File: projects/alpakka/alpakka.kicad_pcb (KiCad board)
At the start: 2 copper layers, 130 x 51 mm, 94 parts, among them P1 Debug, P2 Endpoint, P3 Conn_01x02, Q1 Q_PMOS_DGS, U1 Raspberry_Pico, U10 ST_LSM6, U12 ST_LSM6, U2 Alpsalpine_RKJXV, U3 Alpsalpine_EC10E, U4 Alpsalpine_RKJXM, U6 NXP_PCAL6416A, U8 NXP_PCAL6416A

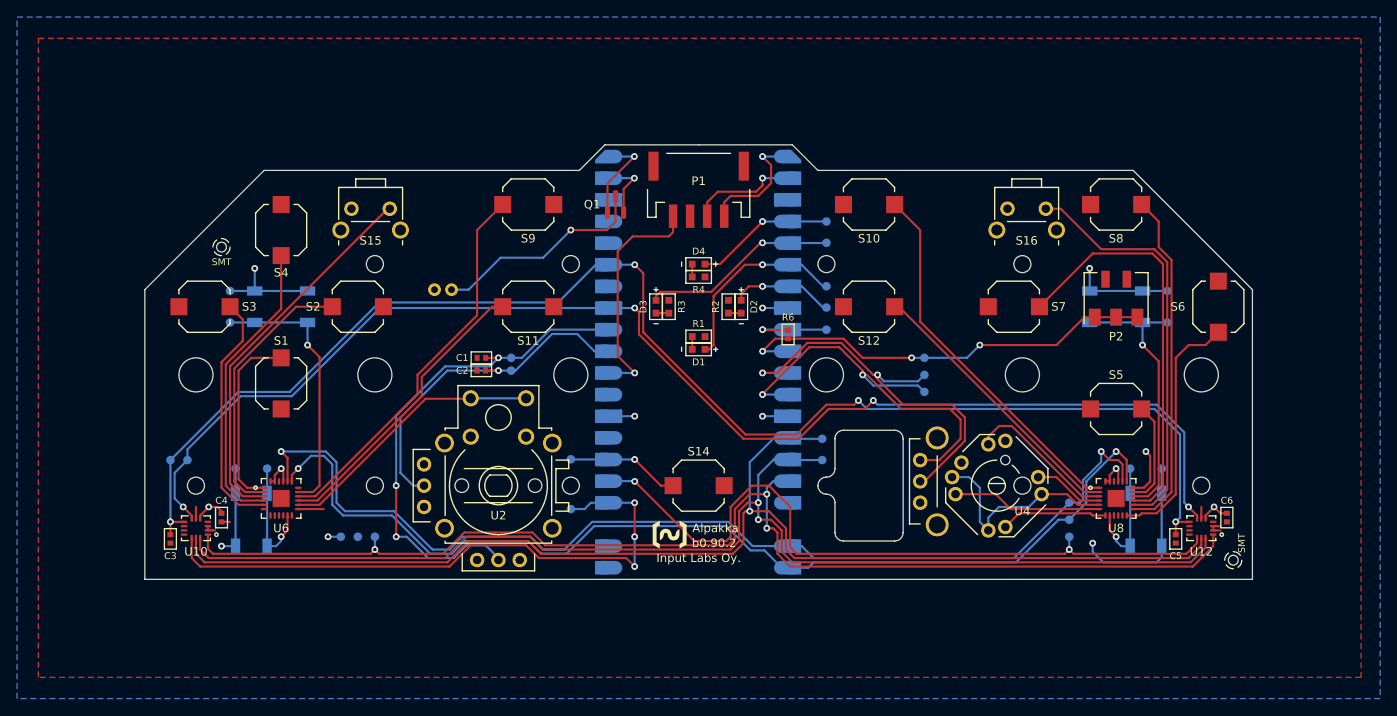
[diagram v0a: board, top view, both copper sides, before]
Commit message: Longmao's dual_thumbstick_mod_for_rp2040_picomini
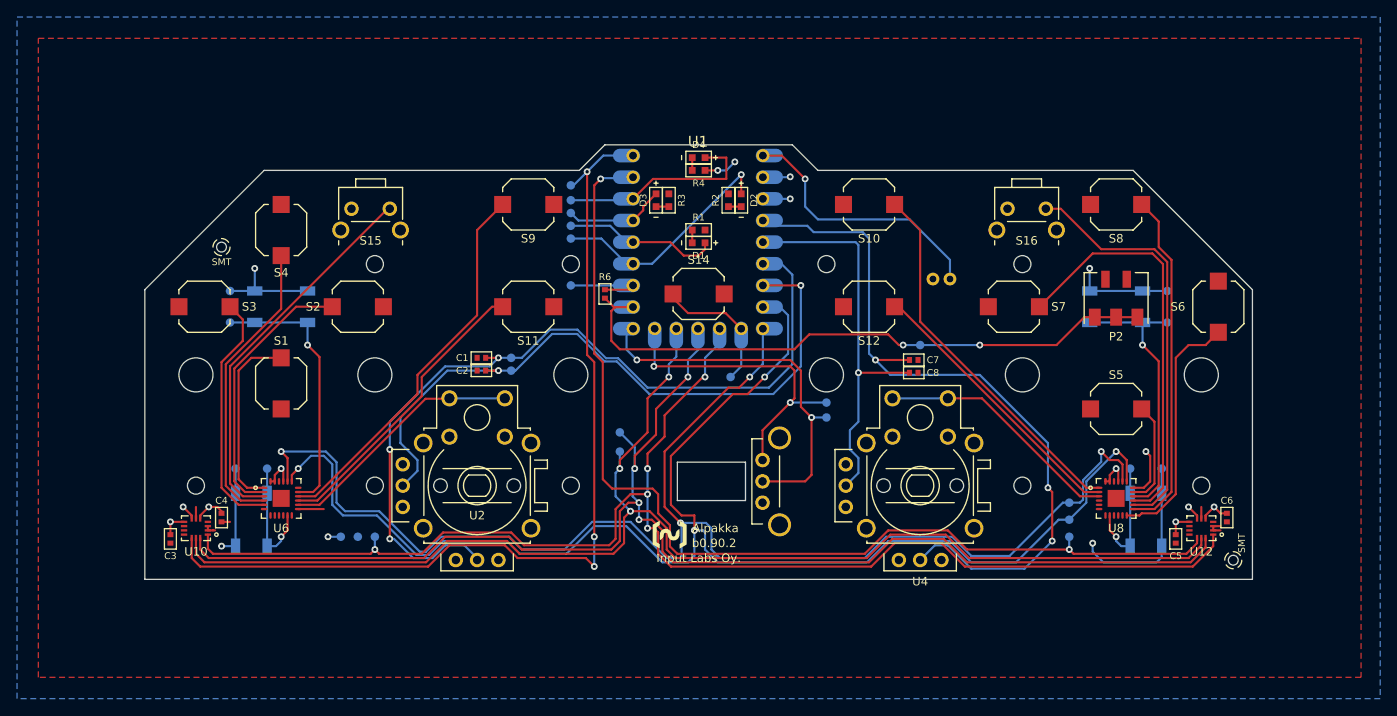
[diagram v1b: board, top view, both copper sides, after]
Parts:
- removed P1: Debug, ILO_fp:JST_S4B-PH-SM4-K-TB
- removed Q1: Q_PMOS_DGS, ILO_fp:SOT-23-DGS
- removed TP33, TP35: Endpoint, ILO_fp:Pad_1mm
- added C7: C, ILO_fp:0402, F.Cu at (125.2, 60.2)
- added C8: C, ILO_fp:0402, F.Cu at (125.2, 61.8)
- U1: value Raspberry_Pico -> 微雪RP2040-ZERO; footprint ILO_fp:Raspberry_Pico -> ILO_fp:PICOMINI
- U4: value Alpsalpine_RKJXM -> Alpsalpine_RKJXV; footprint ILO_fp:Alpsalpine_RKJXM1015004 -> ILO_fp:Alpsalpine_RKJXV122400R
- moved P3 58.5 mm to (128.5, 50.8)
- moved TP0 38.0 mm to (85.0, 39.8)
- moved TP5 31.1 mm to (85.0, 46.0)
- moved TP4 30.8 mm to (85.0, 44.5)
- moved TP6 30.4 mm to (85.0, 51.5)
- moved TP3 30.2 mm to (85.0, 43.0)
- moved TP2 30.1 mm to (85.0, 41.5)
- moved TP11 24.0 mm to (90.8, 68.8)
- moved TP10 23.8 mm to (90.8, 71.0)
- moved S14 22.5 mm to (100.0, 52.5)
- moved R6 22.0 mm to (89.0, 52.5)
- moved TP13 21.1 mm to (103.8, 62.2)
- moved U3 18.5 mm to (108.5, 74.5)
- moved U1 15.1 mm to (100.8, 45.8), turned to 180 degrees
- moved TP8 12.5 mm to (115.0, 67.0)
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- renumbered TP24 to TP0, TP25 to TP1, TP14 to TP10, TP15 to TP11, TP16 to TP12, TP26 to TP13, TP19 to TP14, TP20 to TP15, TP4 to TP2, TP31 to TP26, TP32 to TP27, TP5 to TP3, TP36 to TP3V3, TP6 to TP4, TP7 to TP5, TP9 to TP6, TP10 to TP7, TP11 to TP8, TP12 to TP9, TP3 to TPGND1
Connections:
- C3 pad 2: VCCA -> VCC
- C5 pad 2: VCCA -> VCC
- P3 pad 1: BAT -> 5V
- U1 pad 1: UART_TX -> CS1
- U1 pad 10: GP7 -> SPI_CK
- U1 pad 11: GP8 -> SPI_TX
- U1 pad 12: GP9 -> SPI_RX
- U1 pad 13: GND -> GP20
- U1 pad 14: SPI_CK -> I2C_SDA
- U1 pad 15: SPI_TX -> I2C_SCL
- U1 pad 16: SPI_RX -> ADC0
- U1 pad 17: unconnected-(U1-GP_13-Pad17) -> ADC1
- U1 pad 19: I2C_SDA -> ADC3
- U1 pad 2: UART_RX -> GP2
- U1 pad 20: I2C_SCL -> VCC
- U1 pad 21: unconnected-(U1-GP_16-Pad21) -> GND
- U1 pad 22: unconnected-(U1-GP_17-Pad22) -> 5V
- U1 pad 3: unconnected-(U1-GND-Pad3) -> GP3
- U1 pad 4: GP2 -> GP4
- U1 pad 5: GP3 -> GP5
- U1 pad 6: GP4 -> GP6
- U1 pad 7: GP5 -> GP7
- U1 pad 8: GND -> GP8
- U1 pad 9: GP6 -> GP9
- U10 pad 7: GNDA -> GND
- U10 pad 8: VCCA -> VCC
- U12 pad 7: GNDA -> GND
- U12 pad 8: VCCA -> VCC
- U4 pad 1: B6 -> GND
- U4 pad 2: B3 -> ADC2
- U4 pad 3: B2 -> VCC
- U4 pad 4: B5 -> GND
- U4 pad 5: B4 -> ADC3
- U4 pad 6: GND -> VCC
- U8 pad 4: B3 -> unconnected-(U8-P3-Pad4)
- U8 pad 5: B4 -> unconnected-(U8-P4-Pad5)
- U8 pad 6: B5 -> unconnected-(U8-P5-Pad6)
- U8 pad 7: B6 -> unconnected-(U8-P6-Pad7)
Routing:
- net VCCA: track 167.5 -> 0.00 mm, vias 4 -> 0
- net GNDA: track 155.4 -> 0.00 mm, vias 4 -> 0
- net ADC3: track 0.00 -> 85.8 mm, vias 0 -> 3
- net ADC2: track 0.00 -> 46.3 mm, vias 0 -> 1
- net I2C_SCL: track 121.9 -> 166.9 mm, vias 2 -> 4
- net ADC0: track 40.0 -> 80.3 mm, vias 1 -> 2
- net I2C_SDA: track 124.3 -> 162.9 mm, vias 2 -> 4
- net ADC1: track 58.6 -> 97.1 mm
- net CS0: track 71.8 -> 106.8 mm
- net CS1: track 86.6 -> 121.1 mm
- net 5V: track 0.00 -> 31.2 mm, vias 0 -> 1
- net RUN: track 27.6 -> 0.00 mm, vias 1 -> 0
- net BAT: track 25.5 -> 0.00 mm, vias 1 -> 0
- net B4: track 25.4 -> 0.00 mm
- net GP7: track 51.3 -> 74.7 mm, vias 3 -> 2
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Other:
- outline, holes or cut-outs redrawn
- board text removed: "10"
- board text removed: "13"
- board text removed: "14"
- board text removed: "15"
- board text removed: "16"
- board text removed: "17"
- board text removed: "19"
- board text removed: "20"
- board text removed: "21"
- board text removed: "22"
- board text removed: "24"
- board text removed: "25"
- board text removed: "26"
- board text removed: "27"
- board text removed: "28"
- board text removed: "31"
- board text removed: "32"
- board text removed: "33"
- board text removed: "34"
- board text removed: "36"
- board text removed: "37"
- board text removed: "38"
- board text removed: "39"
- board text removed: "4"
- board text removed: "5"
- board text removed: "7"
- board text removed: "8"
- board text removed: "9"
- board text removed: "USB UP"

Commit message: Cleanup and silkscreen tweaks
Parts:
- removed P3: Conn_01x02, ILO_fp:JST_PH_2_TH
- moved G*** 16.6 mm to (100.0, 64.5)
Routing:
- net 5V: track 31.2 -> 0.00 mm, vias 1 -> 0
- net GP8: track 44.5 -> 41.8 mm
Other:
- outline, holes or cut-outs redrawn
- board text added: "Based on the Alpakka by Input Labs"
- board text added: "CC BY-NC-SA 4.0"
- board text added: "U4"
- board text added: "b0.90.3"
- board text added: "vikkuna"
- board text removed: "2"
- board text removed: "3"
- board text removed: "30"
- board text removed: "Alpakka"
- board text removed: "Input Labs Oy."
- board text removed: "b0.90.2"
